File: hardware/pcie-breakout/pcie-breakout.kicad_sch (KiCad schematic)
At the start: 2 parts, among them J1 Bus_PCI_Express_x1, J2 Conn_01x10

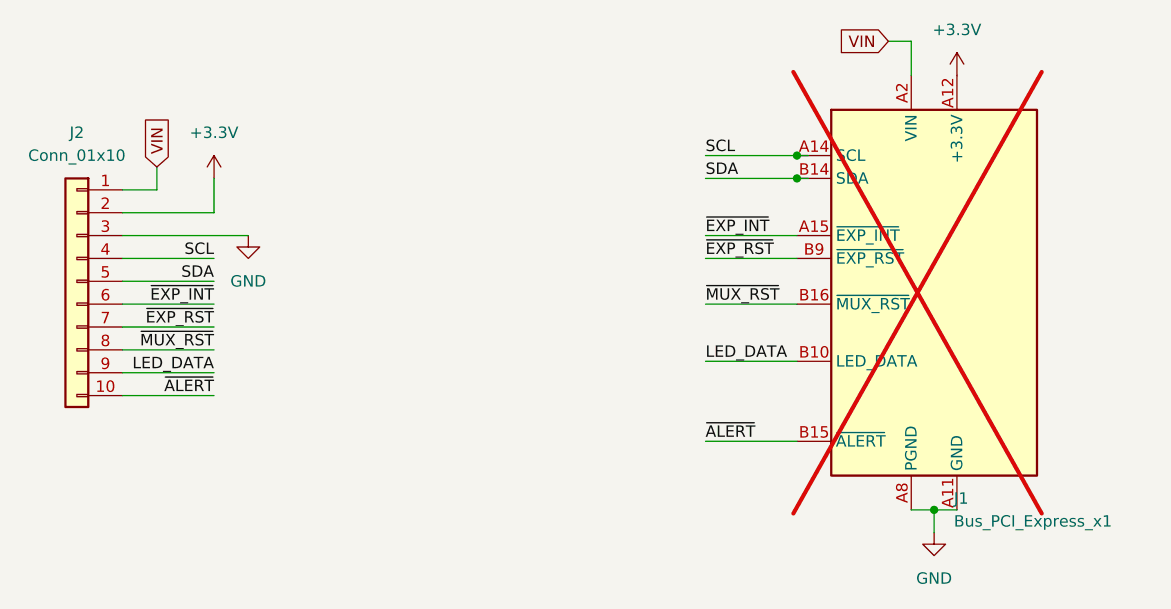
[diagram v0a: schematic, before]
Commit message: chore(pcie-breakout): update 3.3v in to 5v
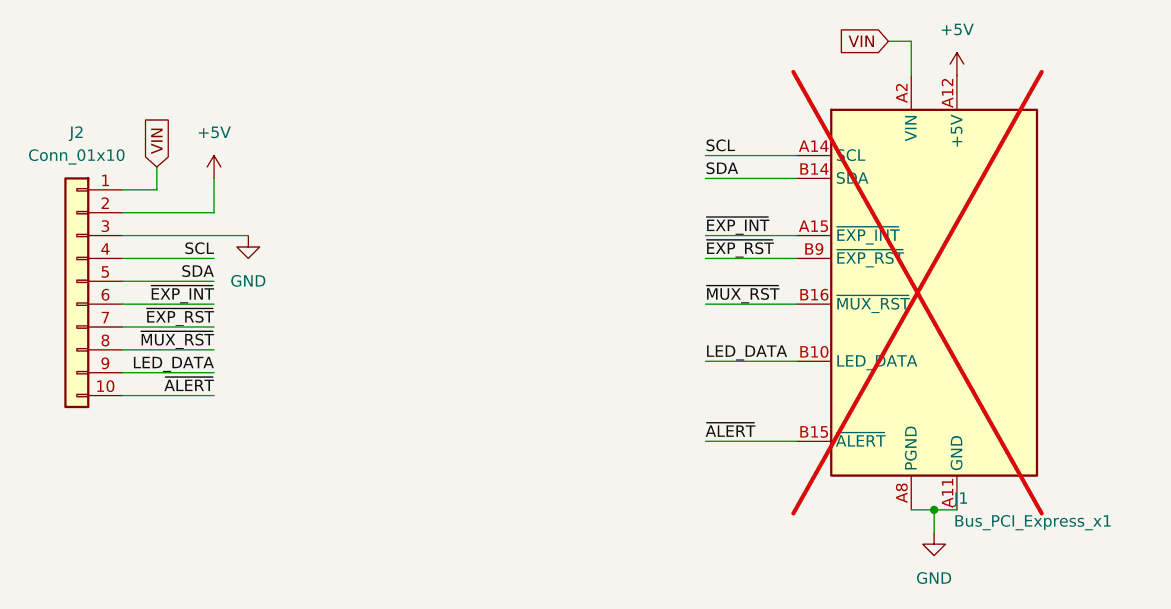
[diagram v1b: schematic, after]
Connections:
- net +3.3V renamed +5V
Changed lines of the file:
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@@
 	(paper "A4")
-	(junction
-		(at 139.7 87.63)
-		(diameter 0)
-		(color 0 0 0 0)
-	)
-	(junction
-		(at 139.7 90.17)
-		(diameter 0)
-		(color 0 0 0 0)
-	)
 	(junction
 		(at 154.94 127)
@@
 	(wire
 		(pts
-			(xy 140.97 87.63) (xy 139.7 87.63)
-		)
-		(stroke
-			(width 0)
-			(type default)
-		)
-	)
-	(wire
-		(pts
 			(xy 129.54 104.14) (xy 139.7 104.14)
 		)
@@
 		(pts
 			(xy 68.58 91.44) (xy 68.58 88.9)
-		)
-		(stroke
-			(width 0)
-			(type default)
-		)
-	)
-	(wire
-		(pts
-			(xy 140.97 90.17) (xy 139.7 90.17)
 		)
 		(stroke
@@
 	)
 	(symbol
-		(lib_id "power:+3.3V")
+		(lib_id "power:+5V")
 		(at 157.48 78.74 0)
 		(unit 1)
@@
 			)
 		)
-		(property "Value" "+3.3V"
+		(property "Value" "+5V"
 			(at 157.48 73.66 0)
 			(show_name no)
@@
 			)
 		)
-		(property "Description" "Power symbol creates a global label with name \"+3.3V\""
+		(property "Description" "Power symbol creates a global label with name \"+5V\""
 			(at 157.48 78.74 0)
 			(hide yes)
@@
 	)
 	(symbol
-		(lib_id "power:+3.3V")
+		(lib_id "power:+5V")
 		(at 74.93 90.17 0)
 		(unit 1)
@@
 			)
 		)
-		(property "Value" "+3.3V"
+		(property "Value" "+5V"
 			(at 74.93 85.09 0)
 			(show_name no)
@@
 			)
 		)
-		(property "Description" "Power symbol creates a global label with name \"+3.3V\""
+		(property "Description" "Power symbol creates a global label with name \"+5V\""
 			(at 74.93 90.17 0)
 			(hide yes)
